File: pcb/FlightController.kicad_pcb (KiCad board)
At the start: 4 copper layers, 36 x 36 mm, 51 parts, among them P2 USB_OTG, P3 CONN_02X04, P4 CKD_SANDWICH, P5 CONN_02X10, Q3 Q_NMOS_DGS, Q4 Q_NMOS_DGS, SW1 SW_PUSH, U1 MPU-6500, U2 STM32F303x{B,C}, U3 TLV70233DBV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

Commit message: v2 of the f3fc which adds pull up resistors for the i2c lines.
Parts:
- removed the G*** at (139.8, 111.1)
- added RP1: R_PACK4, Resistors_SMD:R_Array_Convex_4x1206, B.Cu at (134.2, 110.4)
- moved R5 0.81 mm to (146.0, 109.2)
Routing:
- net /xi2c_SDA: track 14.3 -> 29.3 mm, vias 0 -> 1
- net /xi2c_SCL: track 14.4 -> 29.1 mm, vias 0 -> 1
- net VDD: track 67.0 -> 79.8 mm, vias 17 -> 18
- net /si2c_SDA: track 28.5 -> 38.2 mm, vias 2 -> 3
- net /si2c_SCL: track 27.8 -> 36.5 mm, vias 2 -> 3
- net /TIM15_CH1: track 27.9 -> 31.8 mm
- net /TIM15_CH2: track 35.1 -> 33.2 mm, vias 3 -> 5
- net /Reset/BOOT0: track 25.3 -> 27.2 mm
- net /TIM8_CH2: track 31.5 -> 29.9 mm
- net /TIM1_CH3: track 12.8 -> 13.3 mm
- net /TIM1_CH2: track 14.8 -> 15.3 mm
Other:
- board text added: "ckd.tech/f3fc/v2"
- board text removed: "ckd.tech/f3fc/v1"

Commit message: v3 of f3fc. Correct mosfet pinout. Add measurement points. Remove MPU. Tweaked pinout with one less SPI.
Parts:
- removed C1: 0.01uf, Capacitors_SMD:C_0603_HandSoldering
- removed C4, C6: 0.1uF, Capacitors_SMD:C_0603_HandSoldering
- removed FID1, FID3, FID4: Fiducial_1mm_Dia_2.54mm_Outer_CopperTop, Fiducials:Fiducial_1mm_Dia_2.54mm_Outer_CopperTop
- removed FID2, FID5, FID6: Fiducial_1mm_Dia_2.54mm_Outer_CopperBottom, Fiducials:Fiducial_1mm_Dia_2.54mm_Outer_CopperBottom
- removed G***: LOGO, chickadee:chickadee_3mm_ss
- removed RP1: R_PACK4, Resistors_SMD:R_Array_Convex_4x1206
- removed U1: MPU-6500, Housings_DFN_QFN:QFN-24-1EP_3x3mm_Pitch0.4mm
- added D5: PWR, LEDs:LED-0603, B.Cu at (158.4, 91.8)
- added P1: 3V3, Measurement_Points:Measurement_Point_Round-SMD-Pad_Small, F.Cu at (133.9, 99.5)
- added P10: SWDIO, Measurement_Points:Measurement_Point_Round-SMD-Pad_Small, B.Cu at (141.7, 108.8)
- added P11: SWCLK, Measurement_Points:Measurement_Point_Round-SMD-Pad_Small, B.Cu at (139.6, 108.8)
- added P6: RESET, Measurement_Points:Measurement_Point_Round-SMD-Pad_Small, B.Cu at (164.1, 120.5)
- added P7: BOOT0, Measurement_Points:Measurement_Point_Round-SMD-Pad_Small, B.Cu at (164.1, 118.4)
- added P8: GND, Measurement_Points:Measurement_Point_Square-SMD-Pad_Small, F.Cu at (133.9, 97.3)
- added P9: 5V, Measurement_Points:Measurement_Point_Round-SMD-Pad_Small, F.Cu at (163.5, 97.1)
- added R11: 4.7k, Resistors_SMD:R_0603_HandSoldering, B.Cu at (133.9, 112.2)
- added R12: 1k, Resistors_SMD:R_0603_HandSoldering, B.Cu at (155.4, 92.4)
- added R4: 4.7k, Resistors_SMD:R_0603_HandSoldering, B.Cu at (133.9, 110.3)
- D4: value D_Schottky_x2_KCom_AKA -> D_Schottky_x2_KCom_AAK
- P2: footprint Mini-USB-B -> fci:Mini-USB-B
- Q3, Q4: value Q_NMOS_DGS -> Q_NMOS_GSD
- turned Q4 to 180 degrees
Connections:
- net /TIM8_CH2 renamed /TIM8_CH2_SWCLK
- D4 pad 2: Net-(C11-Pad1) -> +5VA
- D4 pad 3: +5VA -> Net-(C11-Pad1)
- P4 pad 10: /xi2c_SCL -> /PB7
- P4 pad 5: /GPIO1 -> /SWDIO_13
- P4 pad 6: /GPIO2 -> /GPIO1_5
- P4 pad 65: Net-(P4-Pad65) -> /Reset/BOOT0
- P4 pad 66: Net-(P4-Pad66) -> /Reset/RESET
- P4 pad 7: /GPIO3 -> /GPIO2_4
- P4 pad 8: /GPIO4 -> /GPIO3_3
- P4 pad 9: /xi2c_SDA -> /GPIO4_2
- Q3 pad 1: Net-(Q3-Pad1) -> /Reset/RESET
- Q3 pad 2: /Reset/RESET -> GNDPWR
- Q3 pad 3: GNDPWR -> Net-(Q3-Pad3)
- Q4 pad 1: VDD -> Net-(C15-Pad1)
- Q4 pad 2: Net-(C15-Pad1) -> /Reset/BOOT0
- Q4 pad 3: /Reset/BOOT0 -> VDD
- R10 pad 2: Net-(Q3-Pad1) -> Net-(Q3-Pad3)
- R9 pad 2: Net-(Q3-Pad1) -> Net-(Q3-Pad3)
- U2 pad 1: /GPIO4 -> /GPIO4_2
- U2 pad 2: /GPIO3 -> /GPIO3_3
- U2 pad 29: /SPI1_NSS -> Net-(U2-Pad29)
- U2 pad 3: /GPIO2 -> /GPIO2_4
- U2 pad 30: /SPI1_SCK -> Net-(U2-Pad30)
- U2 pad 31: /SPI1_MISO -> Net-(U2-Pad31)
- U2 pad 32: /SPI1_MOSI -> Net-(U2-Pad32)
- U2 pad 33: /MPU_INT -> Net-(U2-Pad33)
- U2 pad 4: /GPIO1 -> /GPIO1_5
- U2 pad 72: Net-(U2-Pad72) -> /SWDIO_13
- U2 pad 92: /xi2c_SCL -> Net-(U2-Pad92)
- U2 pad 93: /xi2c_SDA -> /PB7
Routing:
- net /SWDIO_13: track 0.00 -> 32.5 mm, vias 0 -> 3
- net /xi2c_SDA: track 29.3 -> 0.00 mm, vias 1 -> 0
- net /xi2c_SCL: track 29.1 -> 0.00 mm, vias 1 -> 0
- net /Reset/RESET: track 76.4 -> 101.9 mm, vias 1 -> 2
- net /Reset/BOOT0: track 27.2 -> 49.8 mm, vias 4 -> 7
- net /SPI1_MOSI: track 17.3 -> 0.00 mm
- net /GPIO1: track 15.7 -> 0.00 mm
- net /GPIO1_5: track 0.00 -> 15.6 mm
- net /SPI1_SCK: track 15.1 -> 0.00 mm
- net /GPIO2_4: track 0.00 -> 14.9 mm
- net /PB7: track 0.00 -> 14.9 mm
- net /GPIO2: track 14.6 -> 0.00 mm
- net /GPIO3_3: track 0.00 -> 14.3 mm
- net /GPIO3: track 14.0 -> 0.00 mm
- net /SPI1_NSS: track 13.4 -> 0.00 mm
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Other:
- board text added: "3V3"
- board text added: "5V"
- board text added: "B"
- board text added: "C"
- board text added: "D"
- board text added: "R"
- board text added: "ckd.tech/f3fc/v3"
- board text removed: "ckd.tech/f3fc/v2"

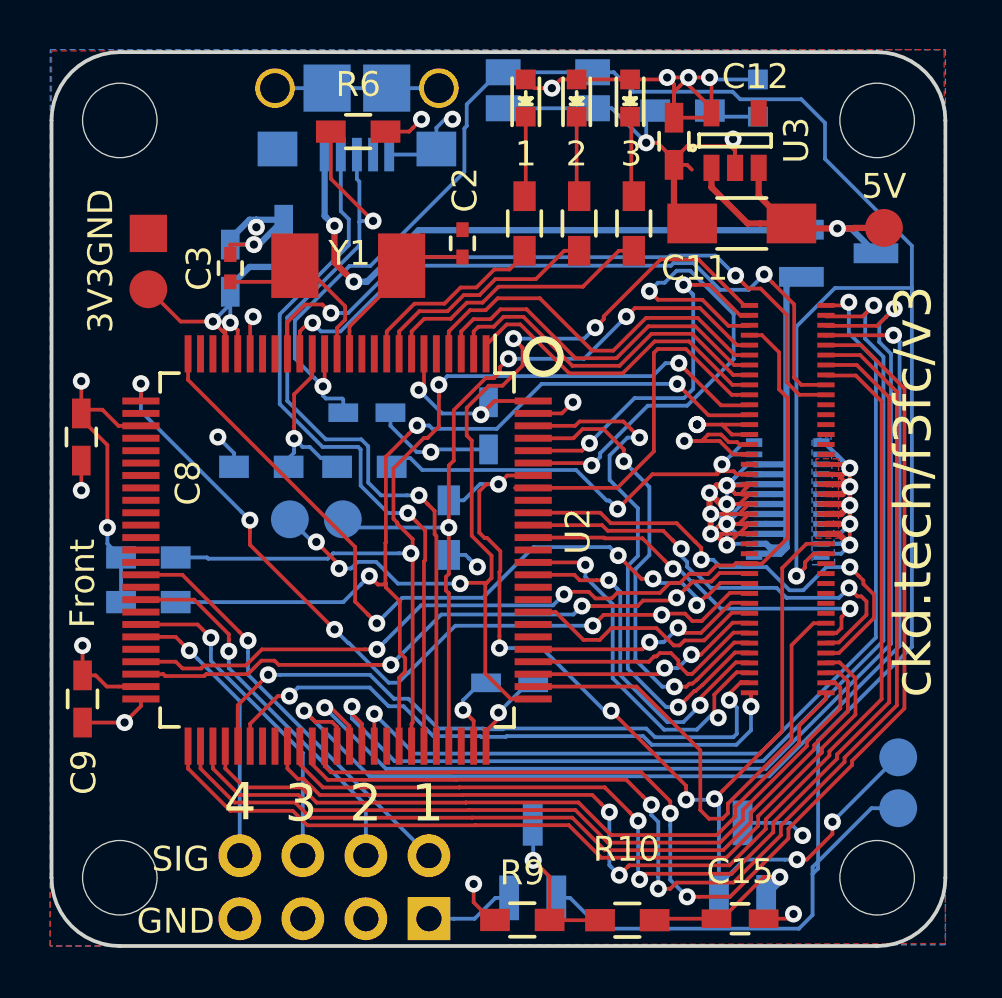
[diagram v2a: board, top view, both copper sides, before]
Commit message: Move decoupling caps to the front side of the board, re-add the MPU and switch from a crystal to a resonator.
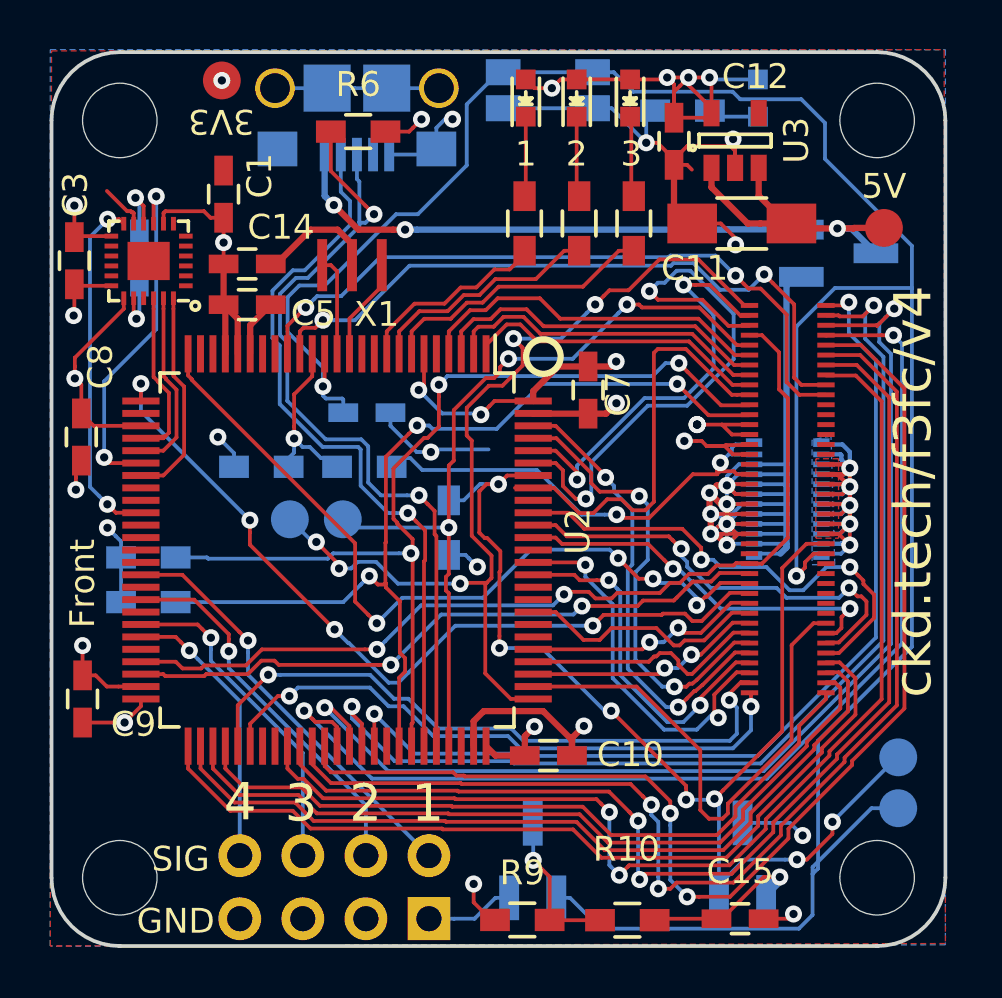
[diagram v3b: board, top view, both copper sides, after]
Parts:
- removed P8: GND, Measurement_Points:Measurement_Point_Square-SMD-Pad_Small
- removed Y1: 8Mhz, abracon:ABM7
- added C1: 10000pF, Capacitors_SMD:C_0603_HandSoldering, F.Cu at (136.9, 95.7)
- added U1: MPU-6500, invensense:QFN-24-1EP_3x3mm_Pitch0.4mm, F.Cu at (133.9, 98.4)
- added X1: 8MHZ, murata-resonator:CSTCE_G-CSTCE_G_Z, F.Cu at (142.1, 98.6)
- C10, C14, C5, C7: moved to F.Cu
- C2: value 27pF -> 0.1uF; footprint Capacitors_SMD:C_0402 -> Capacitors_SMD:C_0603_HandSoldering; moved to B.Cu
- C3: value 27pF -> 0.1uF; footprint Capacitors_SMD:C_0402 -> Capacitors_SMD:C_0603_HandSoldering
- C8, C9: value 100nF -> 0.1uF
- moved C2 13.0 mm to (133.5, 98.3)
- moved P1 8.92 mm to (136.9, 91.1)
- moved C3 6.29 mm to (130.9, 98.4), turned to 270 degrees
- moved C7 4.26 mm to (151.6, 103.6)
- moved C10 3.32 mm to (150.0, 118.3), turned to 0 degrees
- moved C14 1.69 mm to (137.9, 98.5), turned to 180 degrees
- moved C5 1.62 mm to (137.9, 100.2), turned to 180 degrees
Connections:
- C2 pad 1: GNDPWR -> Net-(C2-Pad1)
- C2 pad 2: Net-(C2-Pad2) -> GNDPWR
- C3 pad 1: Net-(C3-Pad1) -> VDD
- U2 pad 12: Net-(C2-Pad2) -> Net-(U2-Pad12)
- U2 pad 13: Net-(C3-Pad1) -> Net-(U2-Pad13)
- U2 pad 29: Net-(U2-Pad29) -> /SPI1_NSS
- U2 pad 30: Net-(U2-Pad30) -> /SPI1_SCK
- U2 pad 31: Net-(U2-Pad31) -> /SPI1_MISO
- U2 pad 32: Net-(U2-Pad32) -> /SPI1_MOSI
- U2 pad 35: Net-(U2-Pad35) -> /MPU_INT
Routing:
- net GNDPWR: track 101.5 -> 117.9 mm
- net /MPU_INT: track 0.00 -> 14.3 mm, vias 0 -> 2
- net /SPI1_MISO: track 0.00 -> 14.1 mm, vias 0 -> 2
- net /SPI1_MOSI: track 0.00 -> 8.57 mm
- net /SPI1_NSS: track 0.00 -> 7.88 mm
- net Net-(C3-Pad1): track 7.62 -> 0.00 mm
- net /SPI1_SCK: track 0.00 -> 7.48 mm
- net Net-(C2-Pad2): track 7.09 -> 0.00 mm
- net VDD: track 72.9 -> 78.3 mm, vias 16 -> 18
- net Net-(U2-Pad12): track 0.00 -> 4.11 mm
- net Net-(U2-Pad13): track 0.00 -> 4.02 mm
- net /UART1_RX: track 21.8 -> 18.5 mm
- net +5VA: track 24.5 -> 21.4 mm
- net Net-(C2-Pad1): track 0.00 -> 2.72 mm, vias 0 -> 1
- net /PB7: track 14.9 -> 17.2 mm
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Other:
- board text added: "ckd.tech/f3fc/v4"
- board text removed: "ckd.tech/f3fc/v3"

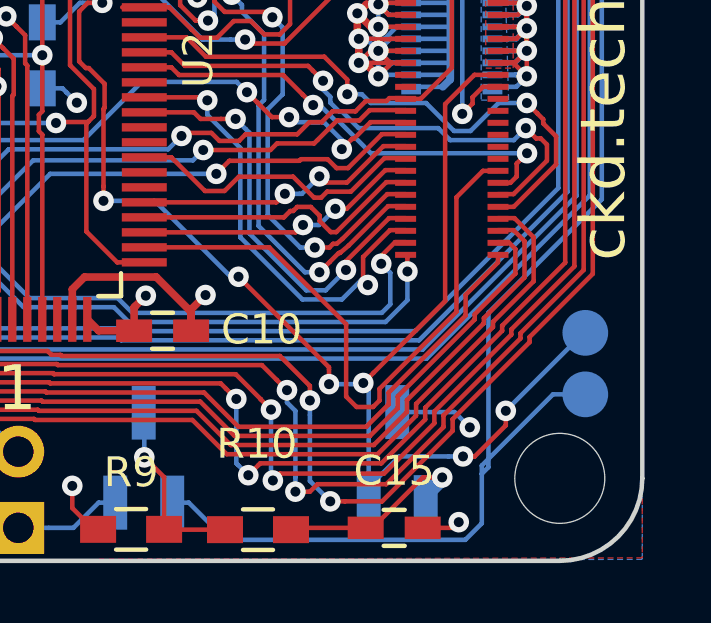
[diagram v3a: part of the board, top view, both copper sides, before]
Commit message: v4 of F3FC including stacking height label
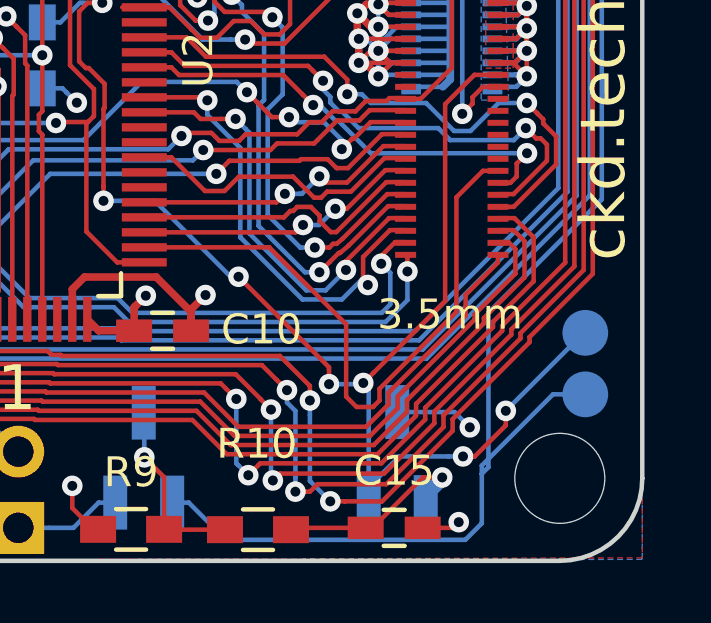
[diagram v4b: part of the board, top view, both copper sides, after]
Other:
- board text added: "3.5mm"
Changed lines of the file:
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@@
-(kicad_pcb (version 4) (host pcbnew "(2015-11-03 BZR 6296)-product")
+(kicad_pcb (version 4) (host pcbnew 4.0.1-stable)
   (general
-    (links 0)
+    (links 201)
     (no_connects 0)
     (area 129.924999 89.924999 166.075001 126.075001)
     (thickness 1.6)
-    (drawings 41)
+    (drawings 42)
     (tracks 1588)
     (zones 0)
@@
       (net 2 GNDPWR))
   )
+  (gr_text 3.5mm (at 159.59 117.79) (layer F.SilkS)
+    (effects (font (size 1 1) (thickness 0.15)))
+  )
   (gr_text 5V (at 163.5252 95.4024) (layer F.SilkS)

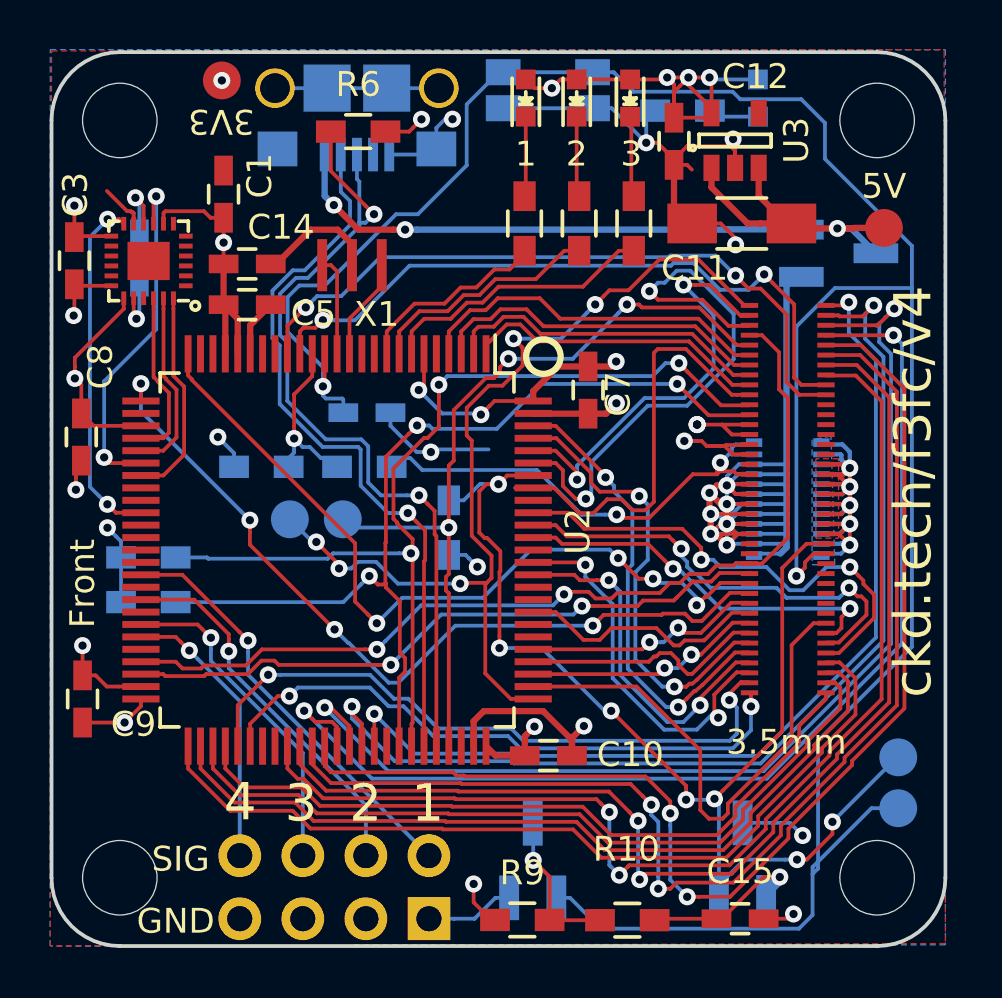
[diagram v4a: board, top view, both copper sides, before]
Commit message: v5 of F3FC. Adjusts motor output location, switches to MPU-6000 and adds chickadee logo back.
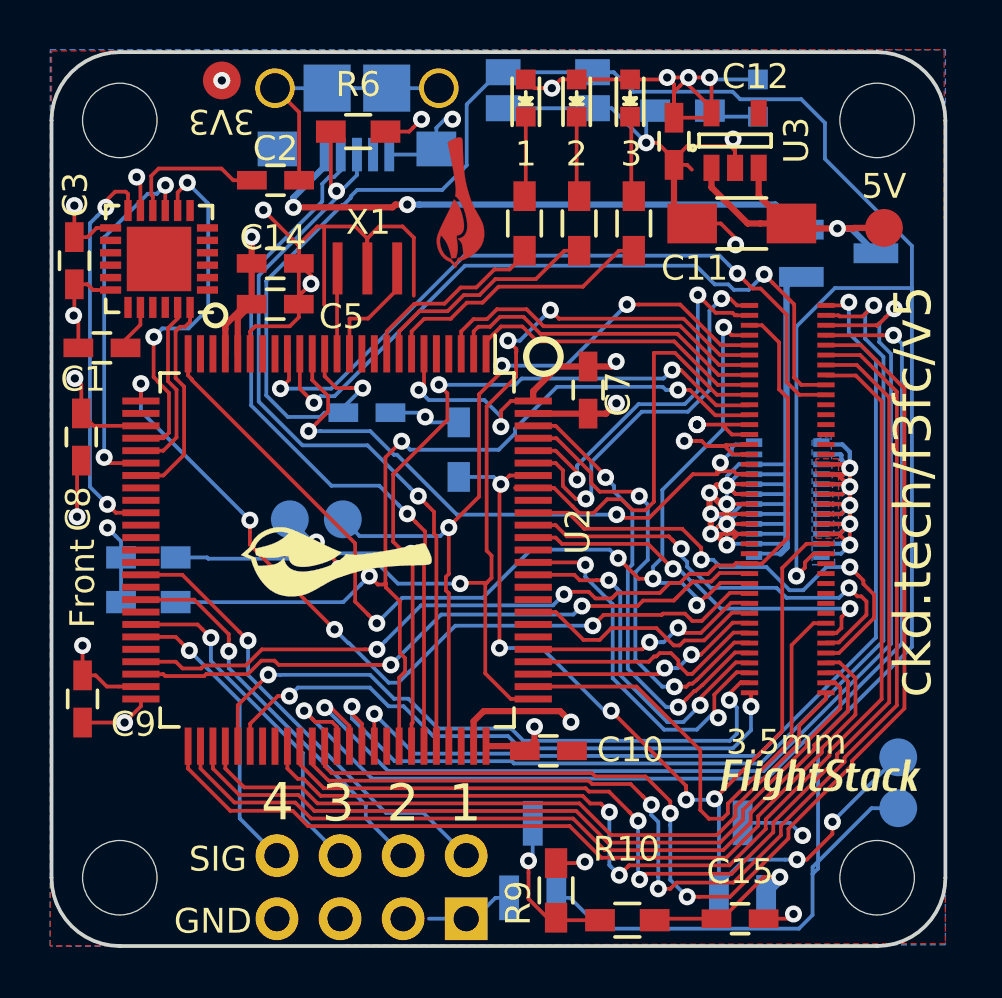
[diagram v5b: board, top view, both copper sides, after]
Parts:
- removed R7: 100k, Resistors_SMD:R_0603_HandSoldering
- removed R8: 10k, Resistors_SMD:R_0603_HandSoldering
- added G***: LOGO, chickadee:chickadee_2mm_fcu, F.Cu at (146.5, 96.1)
- added G***: LOGO, flightstack:flightstack-8mm, F.Cu at (161.0, 119.3)
- added G***: LOGO, chickadee:chickadee_3mm_ss, F.Cu at (141.6, 110.6)
- C1: value 10000pF -> 2.2nF
- C10, C7: value 100nF -> 0.1uF
- C2: moved to F.Cu
- U1: value MPU-6500 -> MPU-6000; footprint invensense:QFN-24-1EP_3x3mm_Pitch0.4mm -> Housings_DFN_QFN:QFN-24-1EP_4x4mm_Pitch0.5mm
- moved C1 7.89 mm to (132.0, 101.9), turned to 0 degrees
- moved C2 6.31 mm to (139.0, 95.2), turned to 0 degrees
- moved R5 3.17 mm to (146.4, 106.0), turned to 270 degrees
- moved R9 1.81 mm to (150.3, 123.8), turned to 270 degrees
- moved P3 1.50 mm to (146.7, 124.9)
- moved C14 1.13 mm to (139.0, 98.5)
- moved C5 1.13 mm to (139.0, 100.2)
- moved X1 0.63 mm to (142.7, 98.7)
- moved U1 0.43 mm to (134.3, 98.3)
- moved C10 0.19 mm to (150.0, 118.1)
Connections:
- C1 pad 1: VDD -> GNDPWR
- C1 pad 2: GNDPWR -> Net-(C1-Pad2)
- P11 pad 1: /TIM8_CH2_SWCLK -> /PA14_SWCLK
- P4 pad 1: /TIM8_CH2_SWCLK -> /TIM16_CH1
- P4 pad 3: /TIM16_CH1 -> /TIM2_CH3
- P4 pad 4: /TIM2_CH3 -> /TIM15_CH1
- P4 pad 6: /GPIO1_5 -> /PA14_SWCLK
- U1 pad 19: VDD -> Net-(U1-Pad19)
- U1 pad 20: GNDPWR -> Net-(C1-Pad2)
- U1 pad 22: /SPI1_NSS -> Net-(U1-Pad22)
- U1 pad 8: VDD -> /SPI1_NSS
- U2 pad 15: /BATT_ADC -> +BATT
- U2 pad 4: /GPIO1_5 -> Net-(U2-Pad4)
- U2 pad 76: /TIM8_CH2_SWCLK -> /PA14_SWCLK
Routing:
- net /TIM8_CH2_SWCLK: track 38.8 -> 0.00 mm, vias 5 -> 0
- net /PA14_SWCLK: track 0.00 -> 36.9 mm, vias 0 -> 5
- net GNDPWR: track 117.9 -> 132.5 mm
- net /GPIO1_5: track 14.5 -> 0.00 mm
- net /TIM15_CH1: track 31.7 -> 44.2 mm, vias 4 -> 5
- net /SPI1_NSS: track 7.88 -> 15.7 mm, vias 0 -> 2
- net +BATT: track 19.5 -> 27.0 mm, vias 2 -> 3
- net /TIM16_CH1: track 23.0 -> 16.1 mm
- net VDD: track 78.3 -> 71.4 mm
- net /BATT_ADC: track 6.65 -> 0.00 mm, vias 1 -> 0
- net /Reset/RESET: track 102.8 -> 108.5 mm
- net Net-(C2-Pad1): track 2.72 -> 5.79 mm, vias 1 -> 0
- net +5VA: track 21.4 -> 23.6 mm
- net /USB_DP: track 34.6 -> 32.6 mm
- net Net-(C1-Pad2): track 0.00 -> 1.88 mm
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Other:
- rule via_min_drill: 0.3 -> 0.3302
- rule via_min_size: 0.3302 -> 0.6858
- board text added: "ckd.tech/f3fc/v5"
- board text removed: "ckd.tech/f3fc/v4"
